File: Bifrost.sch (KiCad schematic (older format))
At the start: 23 parts, among them IC1 DS1085Z-10+, IC2 DS1085Z-10+, J1 OIP, J4 OQP, J5 CalCK

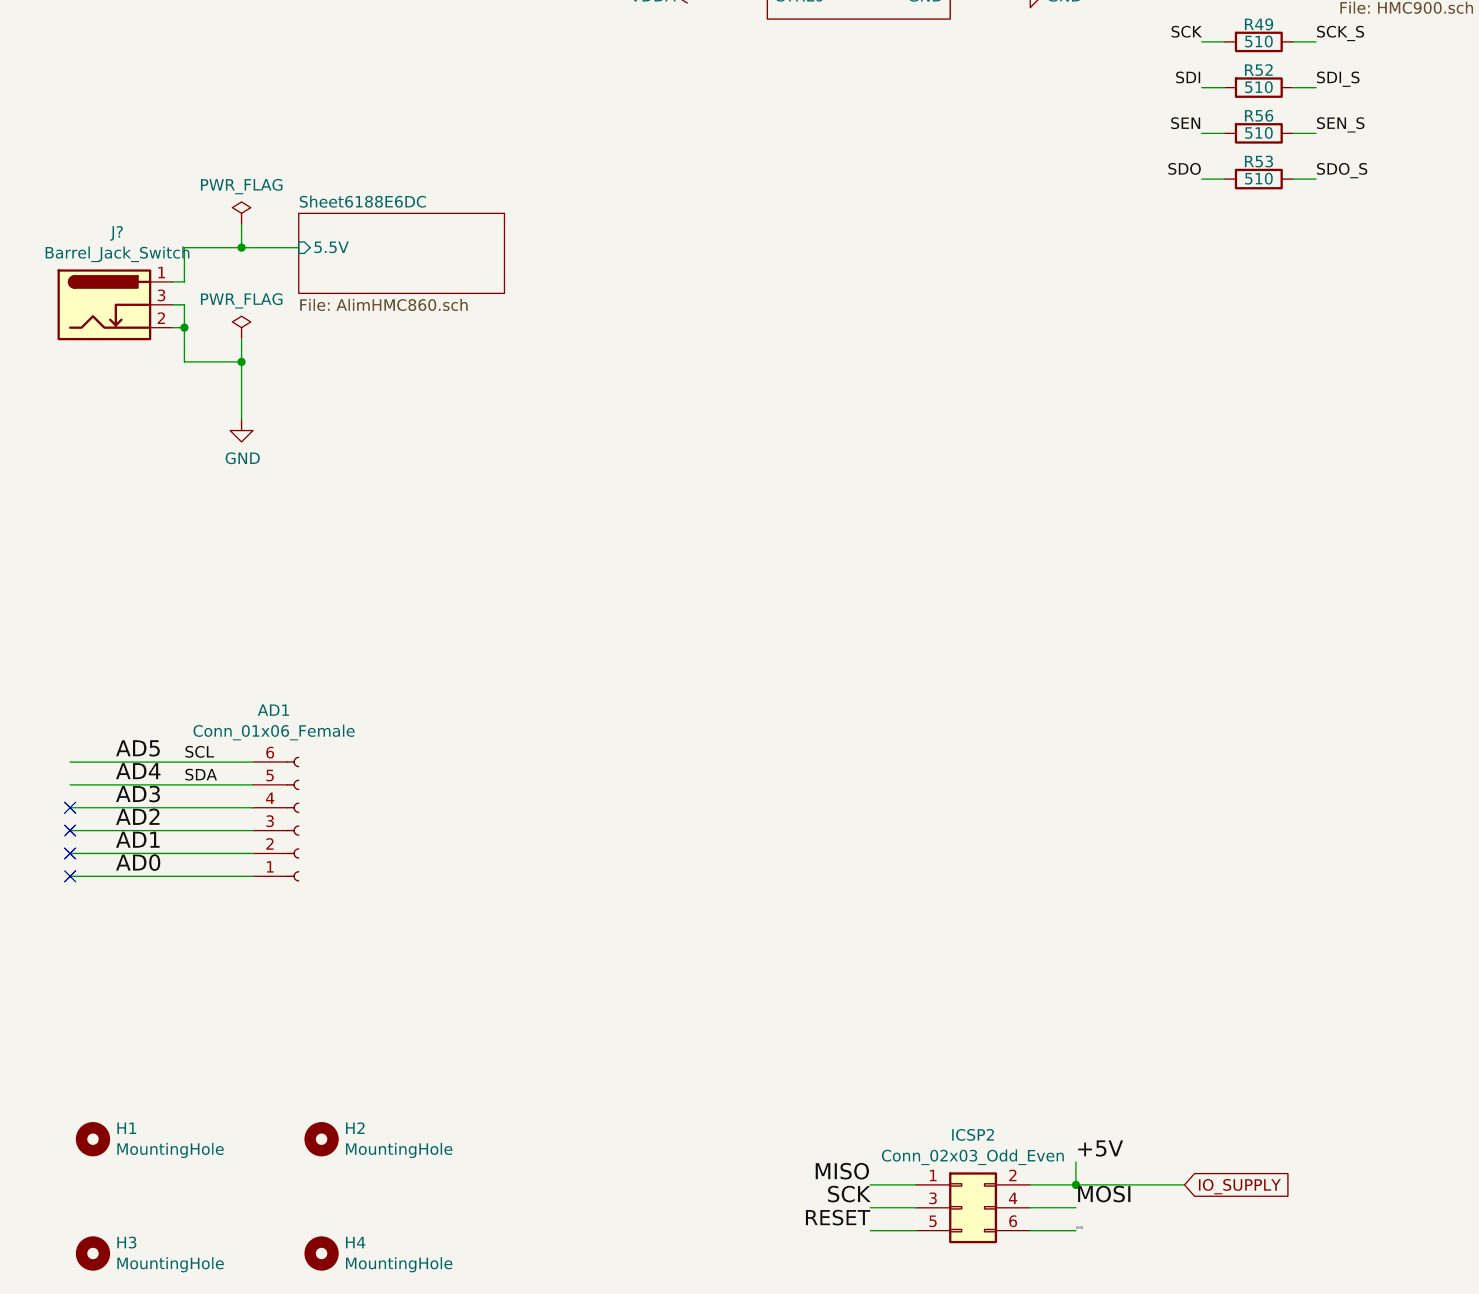
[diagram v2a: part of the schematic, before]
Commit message: Changed power connector to barrel jack and Cal connector to pinhead
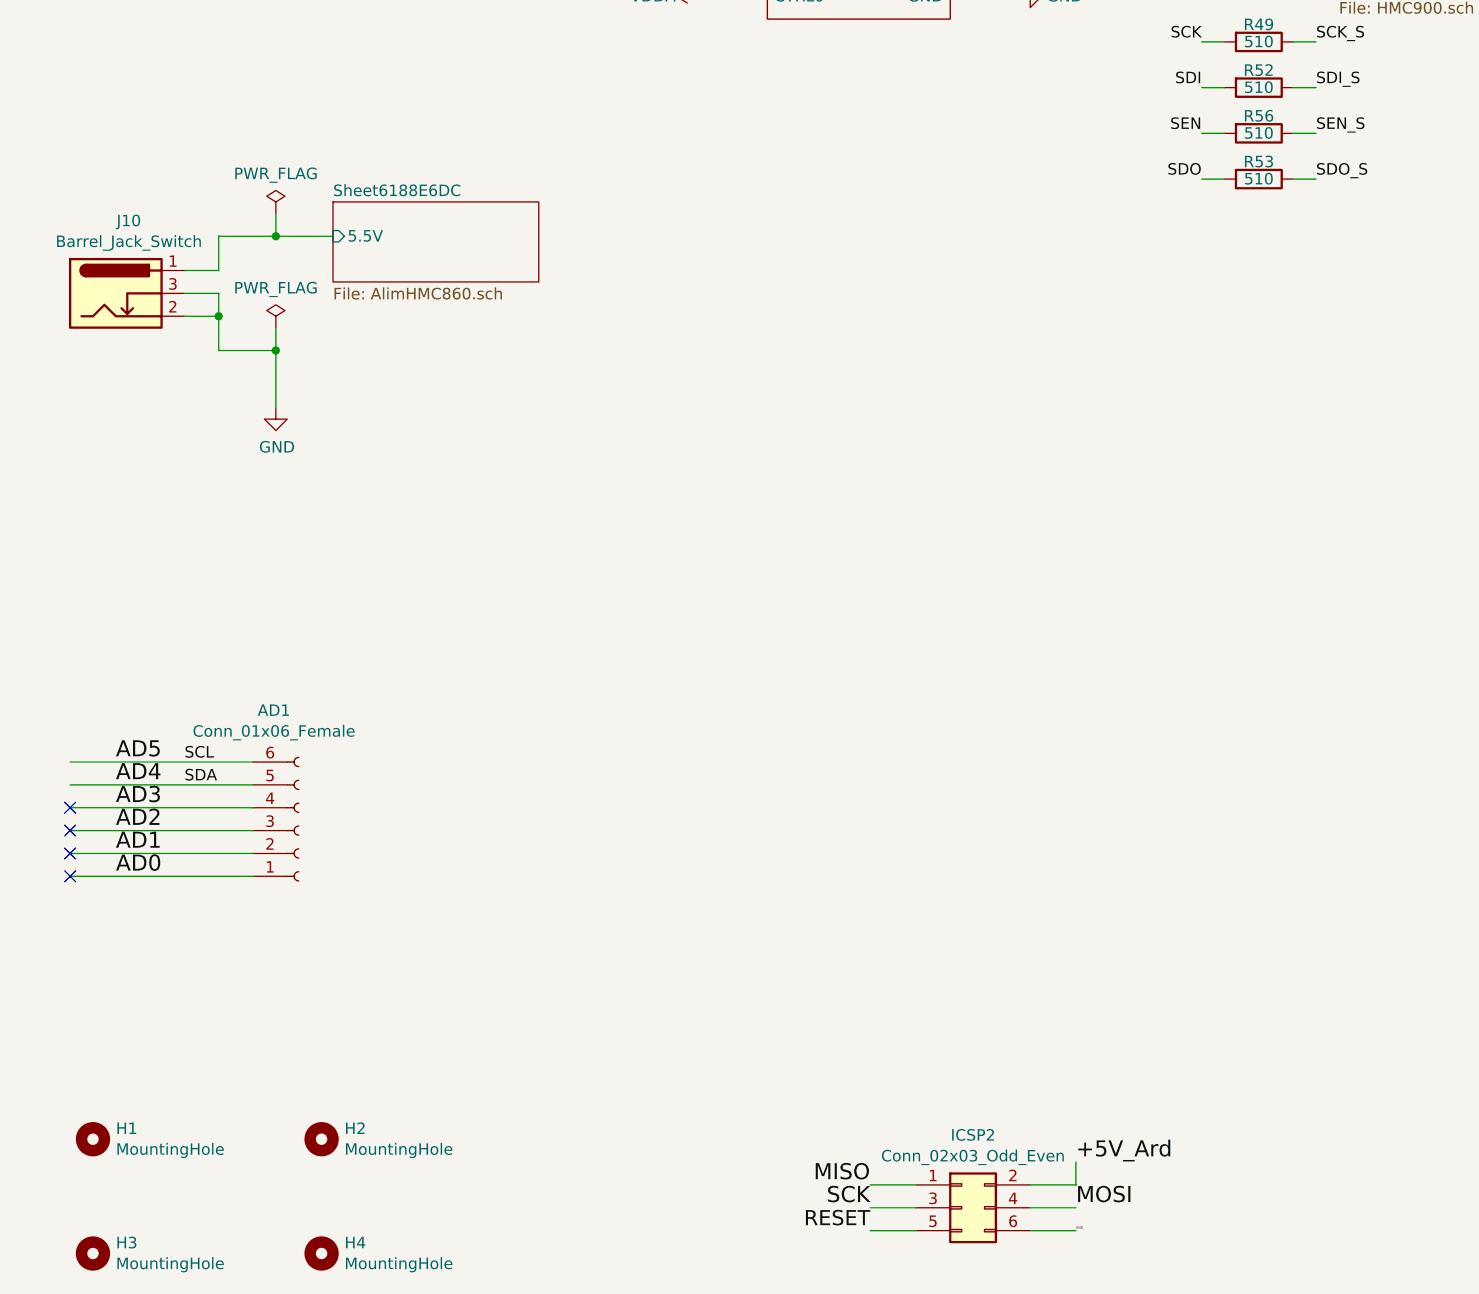
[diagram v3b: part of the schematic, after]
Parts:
- J10: renamed from J?; footprint (none) -> LibPersoNadj:BarrelJack_Swc
- J5: footprint Connector_Coaxial:SMA_Amphenol_132291_Vertical -> Connector_PinHeader_2.54mm:PinHeader_1x02_P2.54mm_Vertical
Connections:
- net labels removed: IO_SUPPLY
- wire segments 106 -> 105
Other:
- moved on the sheet: J10
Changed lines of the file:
@@
 F 0 "J5" H 7750 1875 50  0000 L CNN
 F 1 "CalCK" H 7750 1784 50  0000 L CNN
-F 2 "Connector_Coaxial:SMA_Amphenol_132291_Vertical" H 7650 1900 50  0001 C CNN
+F 2 "Connector_PinHeader_2.54mm:PinHeader_1x02_P2.54mm_Vertical" H 7650 1900 50  0001 C CNN
 F 3 " ~" H 7650 1900 50  0001 C CNN
 	1    7650 1900
@@
 Wire Wire Line
 	7650 2100 7650 2150
-Text GLabel 5475 7350 2    50   Input ~ 0
-IO_SUPPLY
-Wire Wire Line
-	5000 7350 5475 7350
 Wire Wire Line
 	6150 1750 5650 1750
@@
 	7650 1600 7650 1650
 $Sheet
-S 1600 3100 900  350
+S 1750 3050 900  350
 U 6188E6DD
 F0 "Sheet6188E6DC" 50
 F1 "AlimHMC860.sch" 50
-F2 "5.5V" I L 1600 3250 50
+F2 "5.5V" I L 1750 3200 50
 $EndSheet
 Wire Wire Line
-	1600 3250 1350 3250
-Wire Wire Line
-	1350 3750 1100 3750
+	1750 3200 1500 3200
+Wire Wire Line
+	1500 3700 1250 3700
 $Comp
 L power:GND #PWR?
 U 1 1 61AEA5FE
-P 1350 4000
+P 1500 3950
 AR Path="/60D21B6E/61AEA5FE" Ref="#PWR?"  Part="1"
 AR Path="/61AEA5FE" Ref="#PWR0156"  Part="1"
-F 0 "#PWR0156" H 1350 3750 50  0001 C CNN
-F 1 "GND" H 1355 3827 50  0000 C CNN
-F 2 "" H 1350 4000 50  0001 C CNN
-F 3 "" H 1350 4000 50  0001 C CNN
-	1    1350 4000
-	1    0    0    -1
-$EndComp
-Wire Wire Line
-	1350 3750 1350 4000
+F 0 "#PWR0156" H 1500 3700 50  0001 C CNN
+F 1 "GND" H 1505 3777 50  0000 C CNN
+F 2 "" H 1500 3950 50  0001 C CNN
+F 3 "" H 1500 3950 50  0001 C CNN
+	1    1500 3950
+	1    0    0    -1
+$EndComp
+Wire Wire Line
+	1500 3700 1500 3950
 $Comp
 L power:PWR_FLAG #FLG0107
 U 1 1 61B17BC7
-P 1350 3150
-F 0 "#FLG0107" H 1350 3225 50  0001 C CNN
-F 1 "PWR_FLAG" H 1350 3323 50  0000 C CNN
-F 2 "" H 1350 3150 50  0001 C CNN
-F 3 "~" H 1350 3150 50  0001 C CNN
-	1    1350 3150
-	1    0    0    -1
-$EndComp
-Wire Wire Line
-	1350 3150 1350 3250
-Connection ~ 1350 3250
-Wire Wire Line
-	1350 3250 1100 3250
-Wire Wire Line
-	1350 3650 1350 3750
-Connection ~ 1350 3750
+P 1500 3100
+F 0 "#FLG0107" H 1500 3175 50  0001 C CNN
+F 1 "PWR_FLAG" H 1500 3273 50  0000 C CNN
+F 2 "" H 1500 3100 50  0001 C CNN
+F 3 "~" H 1500 3100 50  0001 C CNN
+	1    1500 3100
+	1    0    0    -1
+$EndComp
+Wire Wire Line
+	1500 3100 1500 3200
+Connection ~ 1500 3200
+Wire Wire Line
+	1500 3200 1250 3200
+Wire Wire Line
+	1500 3600 1500 3700
+Connection ~ 1500 3700
 $Comp
 L LibPersoNadj:DS1085Z-10+ IC1
@@
 	5000 7250 5000 7350
 Text Label 5000 7250 0    70   ~ 0
-+5V
++5V_Ard
 Text Label 5000 7550 0    10   ~ 0
 GND
@@
 Text Label 1100 5500 0    50   ~ 0
 SCL
-Connection ~ 5000 7350
 Wire Wire Line
 	5950 2950 6050 2950
@@
 L power:PWR_FLAG #FLG0108
 U 1 1 61B189E4
-P 1350 3650
-F 0 "#FLG0108" H 1350 3725 50  0001 C CNN
-F 1 "PWR_FLAG" H 1350 3823 50  0000 C CNN
-F 2 "" H 1350 3650 50  0001 C CNN
-F 3 "~" H 1350 3650 50  0001 C CNN
-	1    1350 3650
-	1    0    0    -1
-$EndComp
-Wire Wire Line
-	1100 3400 1100 3250
-$Comp
-L Connector:Barrel_Jack_Switch J?
+P 1500 3600
+F 0 "#FLG0108" H 1500 3675 50  0001 C CNN
+F 1 "PWR_FLAG" H 1500 3773 50  0000 C CNN
+F 2 "" H 1500 3600 50  0001 C CNN
+F 3 "~" H 1500 3600 50  0001 C CNN
+	1    1500 3600
+	1    0    0    -1
+$EndComp
+Wire Wire Line
+	1250 3350 1250 3200
+$Comp
+L Connector:Barrel_Jack_Switch J10
 U 1 1 610E86EA
-P 750 3500
-F 0 "J?" H 807 3817 50  0000 C CNN
-F 1 "Barrel_Jack_Switch" H 807 3726 50  0000 C CNN
-F 2 "" H 800 3460 50  0001 C CNN
-F 3 "~" H 800 3460 50  0001 C CNN
-	1    750  3500
-	1    0    0    -1
-$EndComp
-Wire Wire Line
-	1050 3400 1100 3400
-Wire Wire Line
-	1050 3500 1100 3500
-Wire Wire Line
-	1100 3500 1100 3600
-Wire Wire Line
-	1050 3600 1100 3600
-Connection ~ 1100 3600
-Wire Wire Line
-	1100 3600 1100 3750
+P 800 3450
+F 0 "J10" H 857 3767 50  0000 C CNN
+F 1 "Barrel_Jack_Switch" H 857 3676 50  0000 C CNN
+F 2 "LibPersoNadj:BarrelJack_Swc" H 850 3410 50  0001 C CNN
+F 3 "~" H 850 3410 50  0001 C CNN
+	1    800  3450
+	1    0    0    -1
+$EndComp
+Wire Wire Line
+	1100 3350 1250 3350
+Wire Wire Line
+	1100 3450 1250 3450
+Wire Wire Line
+	1250 3450 1250 3550
+Wire Wire Line
+	1100 3550 1250 3550
+Connection ~ 1250 3550
+Wire Wire Line
+	1250 3550 1250 3700
 $EndSCHEMATC

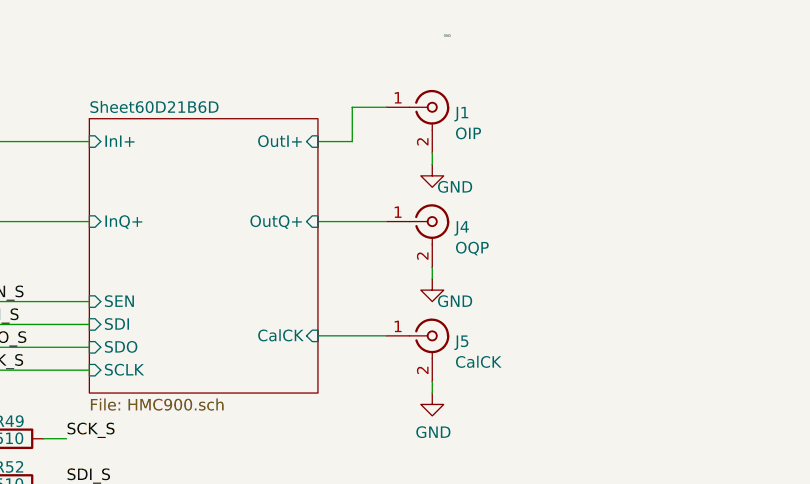
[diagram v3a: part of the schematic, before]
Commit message: Made it so there was only one output and change the SMA (to a sourceable one)
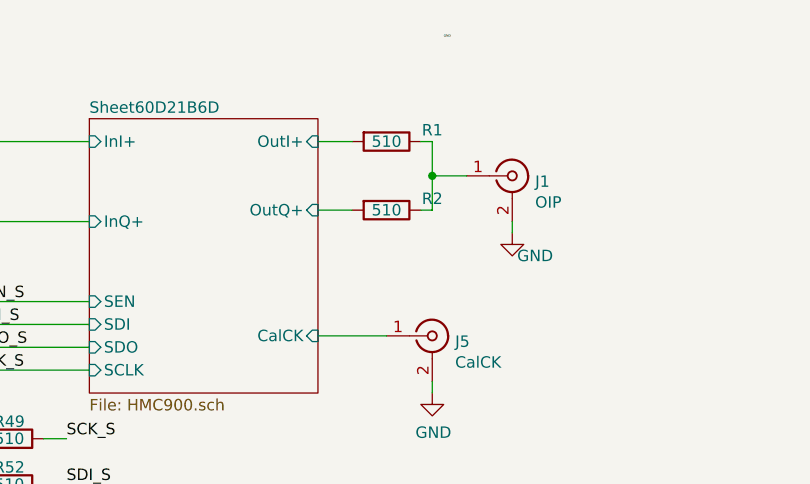
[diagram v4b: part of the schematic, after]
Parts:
- removed J4: OQP, LibPersoNadj:SMA_EdgeMount_Horizontal, symbol Connector:Conn_Coaxial
- added R1, R2: 510, Resistor_SMD:R_0603_1608Metric_Pad0.98x0.95mm_HandSolder, symbol Device:R
- J1: footprint LibPersoNadj:SMA_EdgeMount_Horizontal -> Connector_Coaxial:SMA_Molex_73251-1153_EdgeMount_Horizontal
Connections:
- wire segments 105 -> 107
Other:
- moved on the sheet: J1
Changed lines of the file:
@@
 L Connector:Conn_Coaxial J1
 U 1 1 60C9B584
-P 7650 900
-F 0 "J1" H 7750 875 50  0000 L CNN
-F 1 "OIP" H 7750 784 50  0000 L CNN
-F 2 "LibPersoNadj:SMA_EdgeMount_Horizontal" H 7650 900 50  0001 C CNN
-F 3 " ~" H 7650 900 50  0001 C CNN
-	1    7650 900
-	1    0    0    -1
-$EndComp
-$Comp
-L Connector:Conn_Coaxial J4
-U 1 1 60CA76EC
-P 7650 1400
-F 0 "J4" H 7750 1375 50  0000 L CNN
-F 1 "OQP" H 7750 1284 50  0000 L CNN
-F 2 "LibPersoNadj:SMA_EdgeMount_Horizontal" H 7650 1400 50  0001 C CNN
-F 3 " ~" H 7650 1400 50  0001 C CNN
-	1    7650 1400
+P 8000 1200
+F 0 "J1" H 8100 1175 50  0000 L CNN
+F 1 "OIP" H 8100 1084 50  0000 L CNN
+F 2 "Connector_Coaxial:SMA_Molex_73251-1153_EdgeMount_Horizontal" H 8000 1200 50  0001 C CNN
+F 3 " ~" H 8000 1200 50  0001 C CNN
+	1    8000 1200
 	1    0    0    -1
 $EndComp
@@
 F8 "SCLK" I L 6150 2050 50
 F9 "CalCK" I R 7150 1900 50
-F10 "OutQ+" I R 7150 1400 50
+F10 "OutQ+" I R 7150 1350 50
 $EndSheet
 $Comp
@@
 	7150 1050 7300 1050
 Wire Wire Line
-	7300 1050 7300 900
-Wire Wire Line
-	7300 900  7450 900
+	7650 1200 7800 1200
 $Comp
 L power:GND #PWR?
 U 1 1 617CF474
-P 7650 1150
+P 8000 1450
 AR Path="/60D21B6E/617CF474" Ref="#PWR?"  Part="1"
 AR Path="/617CF474" Ref="#PWR0105"  Part="1"
-F 0 "#PWR0105" H 7650 900 50  0001 C CNN
-F 1 "GND" H 7750 1050 50  0000 C CNN
-F 2 "" H 7650 1150 50  0001 C CNN
-F 3 "" H 7650 1150 50  0001 C CNN
-	1    7650 1150
-	1    0    0    -1
-$EndComp
-Wire Wire Line
-	7650 1100 7650 1150
-$Comp
-L power:GND #PWR?
-U 1 1 617D6611
-P 7650 1650
-AR Path="/60D21B6E/617D6611" Ref="#PWR?"  Part="1"
-AR Path="/617D6611" Ref="#PWR0107"  Part="1"
-F 0 "#PWR0107" H 7650 1400 50  0001 C CNN
-F 1 "GND" H 7750 1550 50  0000 C CNN
-F 2 "" H 7650 1650 50  0001 C CNN
-F 3 "" H 7650 1650 50  0001 C CNN
-	1    7650 1650
-	1    0    0    -1
-$EndComp
-Wire Wire Line
-	7650 1600 7650 1650
+F 0 "#PWR0105" H 8000 1200 50  0001 C CNN
+F 1 "GND" H 8100 1350 50  0000 C CNN
+F 2 "" H 8000 1450 50  0001 C CNN
+F 3 "" H 8000 1450 50  0001 C CNN
+	1    8000 1450
+	1    0    0    -1
+$EndComp
+Wire Wire Line
+	8000 1400 8000 1450
 $Sheet
 S 1750 3050 900  350
@@
 	9950 3150 10550 3150
 Wire Wire Line
-	7150 1400 7450 1400
+	7150 1350 7300 1350
 Text Label 1100 5600 0    50   ~ 0
 SDA
@@
 Wire Wire Line
 	1250 3550 1250 3700
+$Comp
+L Device:R R1
+U 1 1 611AF28E
+P 7450 1050
+F 0 "R1" V 7400 1250 50  0000 C CNN
+F 1 "510" V 7450 1050 50  0000 C CNN
+F 2 "Resistor_SMD:R_0603_1608Metric_Pad0.98x0.95mm_HandSolder" V 7380 1050 50  0001 C CNN
+F 3 "~" H 7450 1050 50  0001 C CNN
+	1    7450 1050
+	0    1    1    0
+$EndComp
+$Comp
+L Device:R R2
+U 1 1 611BB3A9
+P 7450 1350
+F 0 "R2" V 7400 1550 50  0000 C CNN
+F 1 "510" V 7450 1350 50  0000 C CNN
+F 2 "Resistor_SMD:R_0603_1608Metric_Pad0.98x0.95mm_HandSolder" V 7380 1350 50  0001 C CNN
+F 3 "~" H 7450 1350 50  0001 C CNN
+	1    7450 1350
+	0    1    1    0
+$EndComp
+Wire Wire Line
+	7600 1050 7650 1050
+Wire Wire Line
+	7650 1350 7600 1350
+Wire Wire Line
+	7650 1050 7650 1200
+Connection ~ 7650 1200
+Wire Wire Line
+	7650 1200 7650 1350
 $EndSCHEMATC

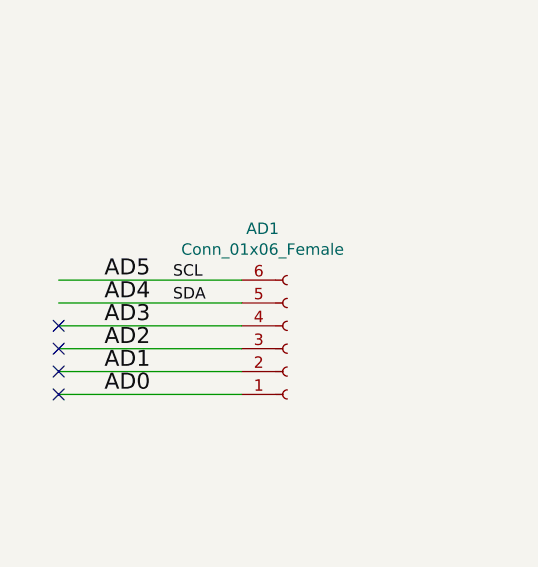
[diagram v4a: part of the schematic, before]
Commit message: Corrected SDA & SCL Pins progressed the routing
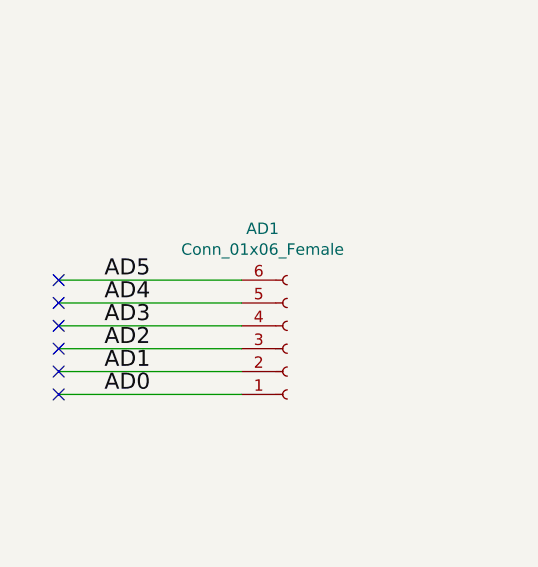
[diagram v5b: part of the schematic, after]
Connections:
- no-connect marks 21 -> 23
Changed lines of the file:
@@
 Wire Wire Line
 	7150 1350 7300 1350
-Text Label 1100 5600 0    50   ~ 0
-SDA
-Text Label 1100 5500 0    50   ~ 0
-SCL
 Wire Wire Line
 	5950 2950 6050 2950
@@
 Wire Wire Line
 	7650 1200 7650 1350
+NoConn ~ 600  5600
+NoConn ~ 600  5500
 $EndSCHEMATC

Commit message: Straitened things before restarting routing
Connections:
- no-connect marks 23 -> 28
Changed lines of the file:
@@
 NoConn ~ 600  5600
 NoConn ~ 600  5500
+NoConn ~ 4100 7350
+NoConn ~ 4100 7450
+NoConn ~ 4100 7550
+NoConn ~ 5000 7450
+NoConn ~ 5000 7250
 $EndSCHEMATC

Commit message: v0 Routing done
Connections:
- net labels added: +5V_Adr_3, +5V_Ard_0, +5V_Ard_1, +5V_Ard_2, MISO_0, MOSI_0, RESET_0, SCK_0
- net labels removed: +5V, +5V_Ard
- wire segments 107 -> 104
- no-connect marks 28 -> 32
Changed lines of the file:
@@
 Wire Wire Line
 	5000 7250 5000 7350
-Text Label 5000 7250 0    70   ~ 0
-+5V_Ard
 Text Label 5000 7550 0    10   ~ 0
 GND
@@
 Text Label 9950 3450 0    70   ~ 0
 SS
-Text Label 9550 1400 0    70   ~ 0
-RESET2
-Text Label 9550 1200 0    70   ~ 0
-MISO2
-Text Label 9550 1300 0    70   ~ 0
-SCK2
 Text Label 800  6000 0    70   ~ 0
 AD0
@@
 Wire Wire Line
 	10700 1400 10700 1500
-Text Label 10700 1300 0    70   ~ 0
-MOSI2
 Wire Wire Line
 	10700 1300 10500 1300
-Text Label 10700 1200 0    10   ~ 0
-+5V
+Text Label 10700 1200 0    21   ~ 0
++5V_Adr_3
 Wire Wire Line
 	10500 1200 10700 1200
-Wire Wire Line
-	10700 1200 10700 1100
 $Comp
 L Mechanical:MountingHole H3
@@
 	1    0    0    -1
 $EndComp
-Text Label 600  1000 0    66   ~ 0
-RESET
 Text Label 7700 600  0    10   ~ 0
 GND
-Wire Wire Line
-	1300 1200 600  1200
-Wire Wire Line
-	1600 1200 1300 1200
-Connection ~ 1300 1200
-Wire Wire Line
-	1300 900  1300 1200
-Wire Wire Line
-	1600 900  1300 900
 $Comp
 L power:GND #PWR0101
@@
 $EndComp
 $Comp
-L power:+5V #PWR0102
-U 1 1 6143901C
-P 10700 1100
-F 0 "#PWR0102" H 10700 950 50  0001 C CNN
-F 1 "+5V" H 10715 1273 50  0000 C CNN
-F 2 "" H 10700 1100 50  0001 C CNN
-F 3 "" H 10700 1100 50  0001 C CNN
-	1    10700 1100
-	1    0    0    -1
-$EndComp
-$Comp
 L power:GND #PWR0103
 U 1 1 61493B4B
@@
 Wire Wire Line
 	600  1000 1600 1000
-Text Label 4100 7550 2    66   ~ 0
-RESET
 Wire Wire Line
 	4100 7550 4300 7550
@@
 Wire Wire Line
 	600  5500 1400 5500
-Text Label 5000 7450 0    70   ~ 0
-MOSI
 Wire Wire Line
 	9950 2950 10550 2950
@@
 Wire Wire Line
 	9950 3550 10550 3550
-Text Label 4100 7350 2    70   ~ 0
-MISO
-Text Label 4100 7450 2    70   ~ 0
-SCK
 Wire Wire Line
 	9950 3150 10550 3150
@@
 NoConn ~ 9950 3650
 Text Label 600  1200 0    21   ~ 0
-+5V_Ard
++5V_Ard_1
 $Comp
 L power:PWR_FLAG #FLG0108
@@
 NoConn ~ 5000 7450
 NoConn ~ 5000 7250
+Text Label 600  1000 0    66   ~ 0
+RESET
+Text Label 9550 1400 0    70   ~ 0
+RESET2
+Text Label 9550 1300 0    70   ~ 0
+SCK2
+Text Label 9550 1200 0    70   ~ 0
+MISO2
+Text Label 10700 1300 0    70   ~ 0
+MOSI2
+Text Label 5000 7250 0    70   ~ 0
++5V_Ard_0
+Text Label 5000 7450 0    70   ~ 0
+MOSI_0
+Text Label 4100 7550 2    66   ~ 0
+RESET_0
+Text Label 4100 7450 2    70   ~ 0
+SCK_0
+Text Label 4100 7350 2    70   ~ 0
+MISO_0
+Text Label 600  900  0    21   ~ 0
++5V_Ard_2
+Wire Wire Line
+	600  900  1600 900
+Wire Wire Line
+	600  1200 1600 1200
+NoConn ~ 600  900
+NoConn ~ 600  1000
+NoConn ~ 600  1200
+NoConn ~ 10700 1200
 $EndSCHEMATC

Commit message: Added BPF-E16+
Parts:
- added RV?: POT_Mod_Freq1, symbol Device:R_POT
- added RV?: POT_Mod_Freq2, symbol Device:R_POT
- added U? (x2): BPF-E16, LibPersoNadj:Mini-Circuits_HR1176, symbol LibPersoNadj:BPF-E16
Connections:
- wire segments 104 -> 118
- no-connect marks 32 -> 30
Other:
- moved on the sheet: AD1, IC1, IC2, J1, J5, R1, R2, R49, R52, R53, R56, R71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
